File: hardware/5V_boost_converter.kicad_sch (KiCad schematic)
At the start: 10 parts, among them U5 TPS61200DRC

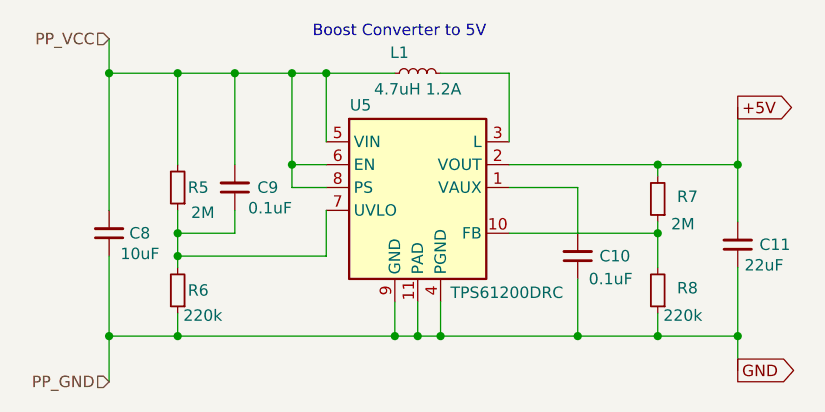
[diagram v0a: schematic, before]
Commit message: Made the global labels for power visible in the main shchematic
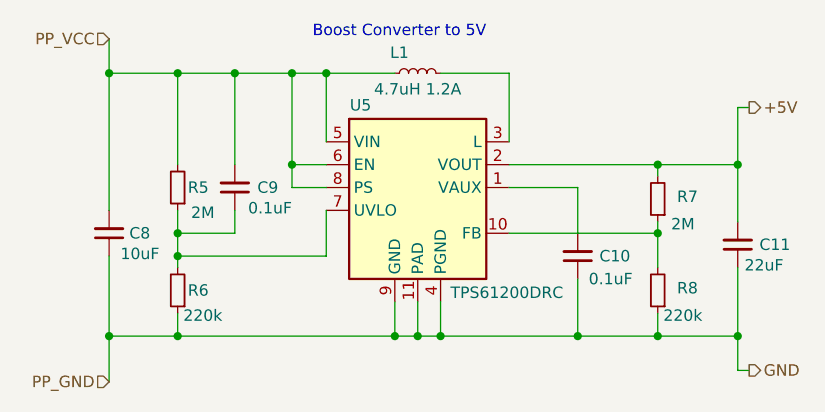
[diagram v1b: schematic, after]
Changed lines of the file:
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@@
+	(wire
+		(pts
+			(xy 175.26 107.95) (xy 176.53 107.95)
+		)
+		(stroke
+			(width 0)
+			(type default)
+		)
+	)
 	(wire
 		(pts
@@
 		(pts
 			(xy 142.24 104.14) (xy 139.7 104.14)
+		)
+		(stroke
+			(width 0)
+			(type default)
+		)
+	)
+	(wire
+		(pts
+			(xy 175.26 78.74) (xy 176.53 78.74)
 		)
 		(stroke
@@
 		)
 	)
-	(global_label "+5V"
+	(hierarchical_label "GND"
 		(shape output)
-		(at 175.26 78.74 0)
+		(at 176.53 107.95 0)
 		(fields_autoplaced yes)
 		(effects
@@
 			)
 			(justify left)
-		)
-		(property "Intersheetrefs" "${INTERSHEET_REFS}"
-			(at 182.1157 78.74 0)
-			(effects
-				(font
-					(size 1.27 1.27)
-				)
-				(justify left)
-				(hide yes)
-			)
-		)
-	)
-	(global_label "GND"
-		(shape output)
-		(at 175.26 107.95 0)
-		(fields_autoplaced yes)
-		(effects
-			(font
-				(size 1.27 1.27)
-			)
-			(justify left)
-		)
-		(property "Intersheetrefs" "${INTERSHEET_REFS}"
-			(at 182.1157 107.95 0)
-			(effects
-				(font
-					(size 1.27 1.27)
-				)
-				(justify left)
-				(hide yes)
-			)
 		)
 	)
@@
 		)
 	)
+	(hierarchical_label "+5V"
+		(shape output)
+		(at 176.53 78.74 0)
+		(fields_autoplaced yes)
+		(effects
+			(font
+				(size 1.27 1.27)
+			)
+			(justify left)
+		)
+	)

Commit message: Minor cosmetic changes
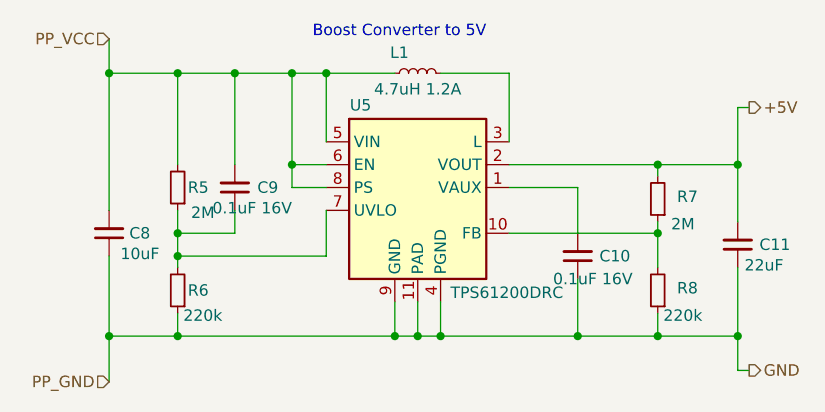
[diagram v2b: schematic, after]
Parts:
- C10, C9: value 0.1uF -> 0.1uF 16V; Package (none) -> 0805; Part Num (none) -> GRM21BR71H104KA01L; Price/unit (none) -> $0.0097; Supplier Link (none) -> https://jlcpcb.com/partdetail/MurataElectronics-GRM21BR71H1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
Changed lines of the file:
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@@
 			)
 		)
-		(property "Value" "0.1uF"
+		(property "Value" "0.1uF 16V"
 			(at 163.576 97.79 0)
 			(effects
@@
 			)
 		)
-		(property "Datasheet" "~"
+		(property "Datasheet" "https://wmsc.lcsc.com/wmsc/upload/file/pdf/v2/lcsc/2304140030_Murata-Electronics-GRM21BR71H104KA01L_C77082.pdf"
 			(at 157.48 95.25 0)
 			(effects
@@
 		)
 		(property "Description" "Unpolarized capacitor, small symbol"
+			(at 157.48 95.25 0)
+			(effects
+				(font
+					(size 1.27 1.27)
+				)
+				(hide yes)
+			)
+		)
+		(property "Package" "0805"
+			(at 157.48 95.25 0)
+			(effects
+				(font
+					(size 1.27 1.27)
+				)
+				(hide yes)
+			)
+		)
+		(property "Part Num" "GRM21BR71H104KA01L"
+			(at 157.48 95.25 0)
+			(effects
+				(font
+					(size 1.27 1.27)
+				)
+				(hide yes)
+			)
+		)
+		(property "Price/unit" "$0.0097"
+			(at 157.48 95.25 0)
+			(effects
+				(font
+					(size 1.27 1.27)
+				)
+				(hide yes)
+			)
+		)
+		(property "Supplier Link" "https://jlcpcb.com/partdetail/MurataElectronics-GRM21BR71H104KA01L/C77082"
 			(at 157.48 95.25 0)
 			(effects
@@
 			)
 		)
-		(property "Value" "0.1uF"
+		(property "Value" "0.1uF 16V"
 			(at 125.73 89.916 0)
 			(effects
@@
 			)
 		)
-		(property "Datasheet" "~"
+		(property "Datasheet" "https://wmsc.lcsc.com/wmsc/upload/file/pdf/v2/lcsc/2304140030_Murata-Electronics-GRM21BR71H104KA01L_C77082.pdf"
 			(at 119.38 87.63 0)
 			(effects
@@
 			(at 119.38 87.63 0)
 			(effects
+				(font
+					(size 1.27 1.27)
+				)
+				(hide yes)
+			)
+		)
+		(property "Package" "0805"
+			(at 119.38 87.63 0)
+			(effects
+				(font
+					(size 1.27 1.27)
+				)
+				(hide yes)
+			)
+		)
+		(property "Part Num" "GRM21BR71H104KA01L"
+			(at 119.38 87.63 0)
+			(effects
+				(font
+					(size 1.27 1.27)
+				)
+				(hide yes)
+			)
+		)
+		(property "Price/unit" "$0.0097"
+			(at 119.38 87.63 0)
+			(effects
+				(font
+					(size 1.27 1.27)
+				)
+				(hide yes)
+			)
+		)
+		(property "Supplier Link" "https://jlcpcb.com/partdetail/MurataElectronics-GRM21BR71H104KA01L/C77082"
+			(at 119.38 87.63 0)
+			(effects

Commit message: Added information, footprints and 3d models for several components
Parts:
- U5: Package (none) -> VSON-10-EP(3x3); Part Num (none) -> TPS61200DRCR; Price/unit (none) -> $1.4430; Supplier Link (none) -> https://jlcpcb.com/partdetail/TexasInstruments-TPS61200DRCR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
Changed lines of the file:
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@@
 			)
 		)
-		(property "Datasheet" "http://www.ti.com/lit/ds/symlink/tps61200.pdf"
+		(property "Datasheet" "https://www.lcsc.com/datasheet/lcsc_datasheet_1809191830_Texas-Instruments-TPS61200DRCR_C140320.pdf"
 			(at 139.7 87.63 0)
 			(effects
@@
 			)
 		)
-		(property "Description" "Low Input Voltage Synchronous Boost Converter With 1.3A Switches, Adjustable Output Voltage, 0.3-5.5V Input Voltage, VSON-10"
+		(property "Description" "Boost type Adjustable 1.8V~5.5V 300mV~5.5V 1.2A VSON-10-EP(3x3) DC-DC Converters ROHS"
 			(at 139.7 87.63 0)
 			(effects
+				(font
+					(size 1.27 1.27)
+				)
+				(hide yes)
+			)
+		)
+		(property "Supplier Link" "https://jlcpcb.com/partdetail/TexasInstruments-TPS61200DRCR/C140320"
+			(at 139.7 87.63 0)
+			(effects
+				(font
+					(size 1.27 1.27)
+				)
+				(hide yes)
+			)
+		)
+		(property "Price/unit" "$1.4430"
+			(at 139.7 87.63 0)
+			(effects
+				(font
+					(size 1.27 1.27)
+				)
+				(hide yes)
+			)
+		)
+		(property "Part Num" "TPS61200DRCR"
+			(at 139.7 87.63 0)
+			(effects
+				(font
+					(size 1.27 1.27)
+				)
+				(hide yes)
+			)
+		)
+		(property "Package" "VSON-10-EP(3x3)"
+			(at 139.7 87.63 0)
+			(effects
